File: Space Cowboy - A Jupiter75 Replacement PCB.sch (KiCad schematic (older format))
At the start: 203 parts, among them SW1 SW_PUSH, U1 ATmega32U4-AU, Y1 16MHz

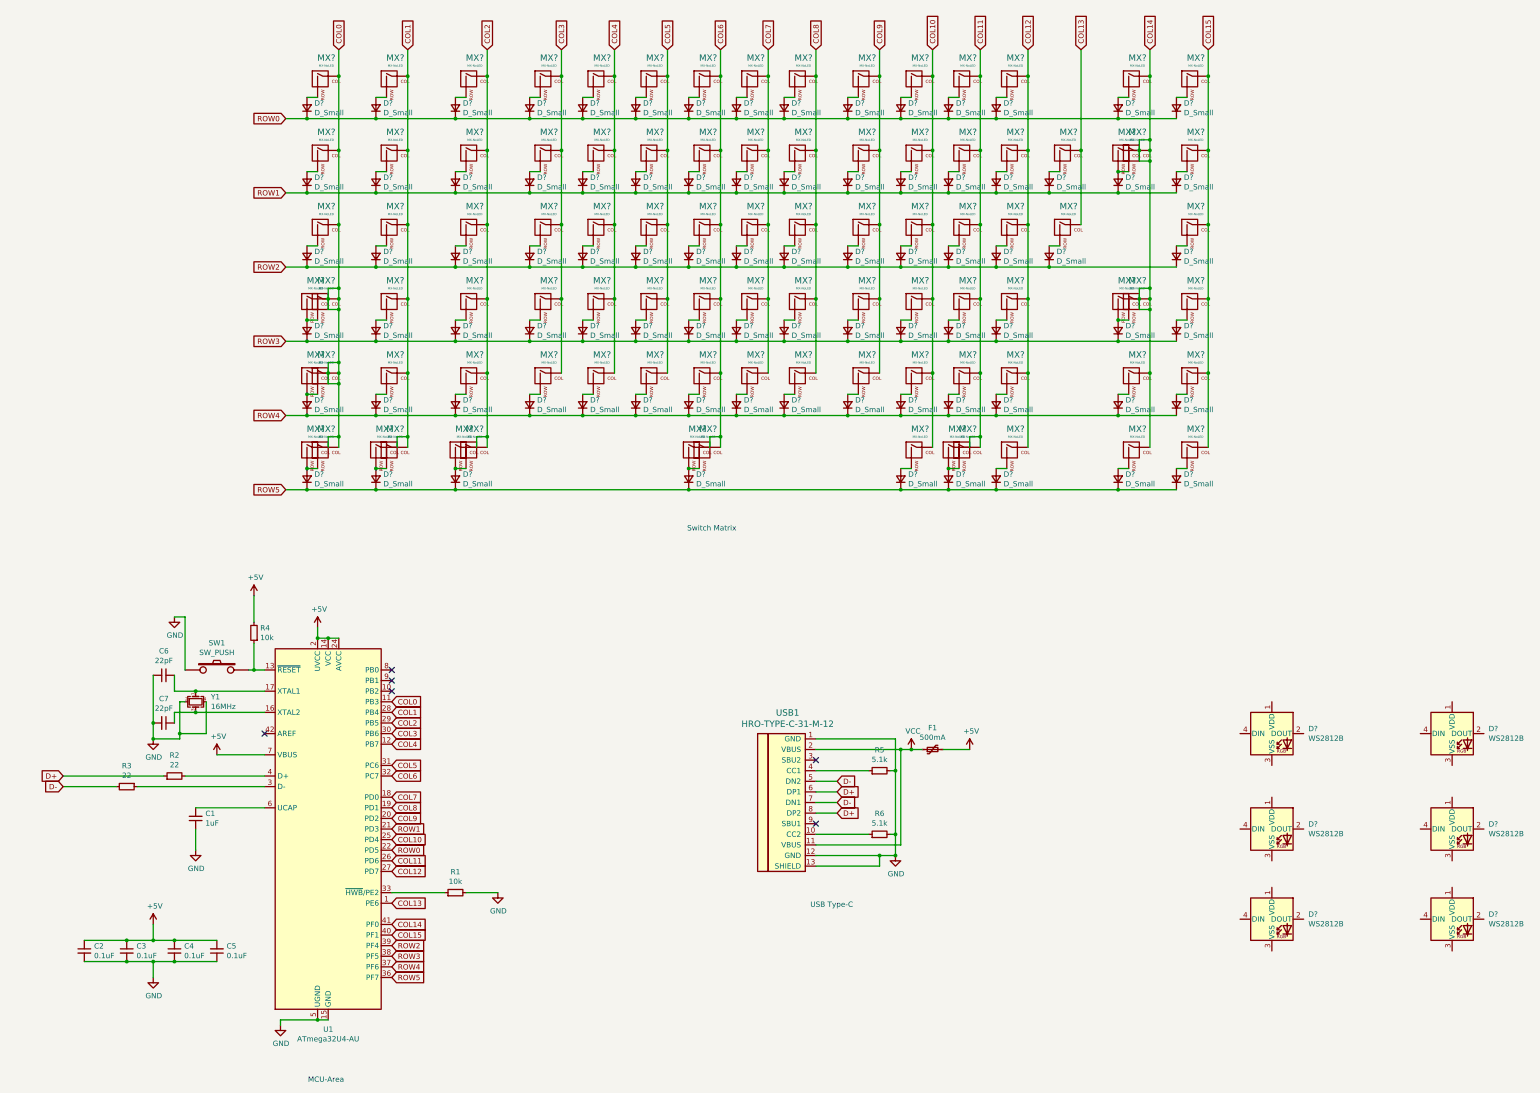
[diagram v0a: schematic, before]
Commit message: Update Space Cowboy - A Jupiter75 Replacement PCB.sch
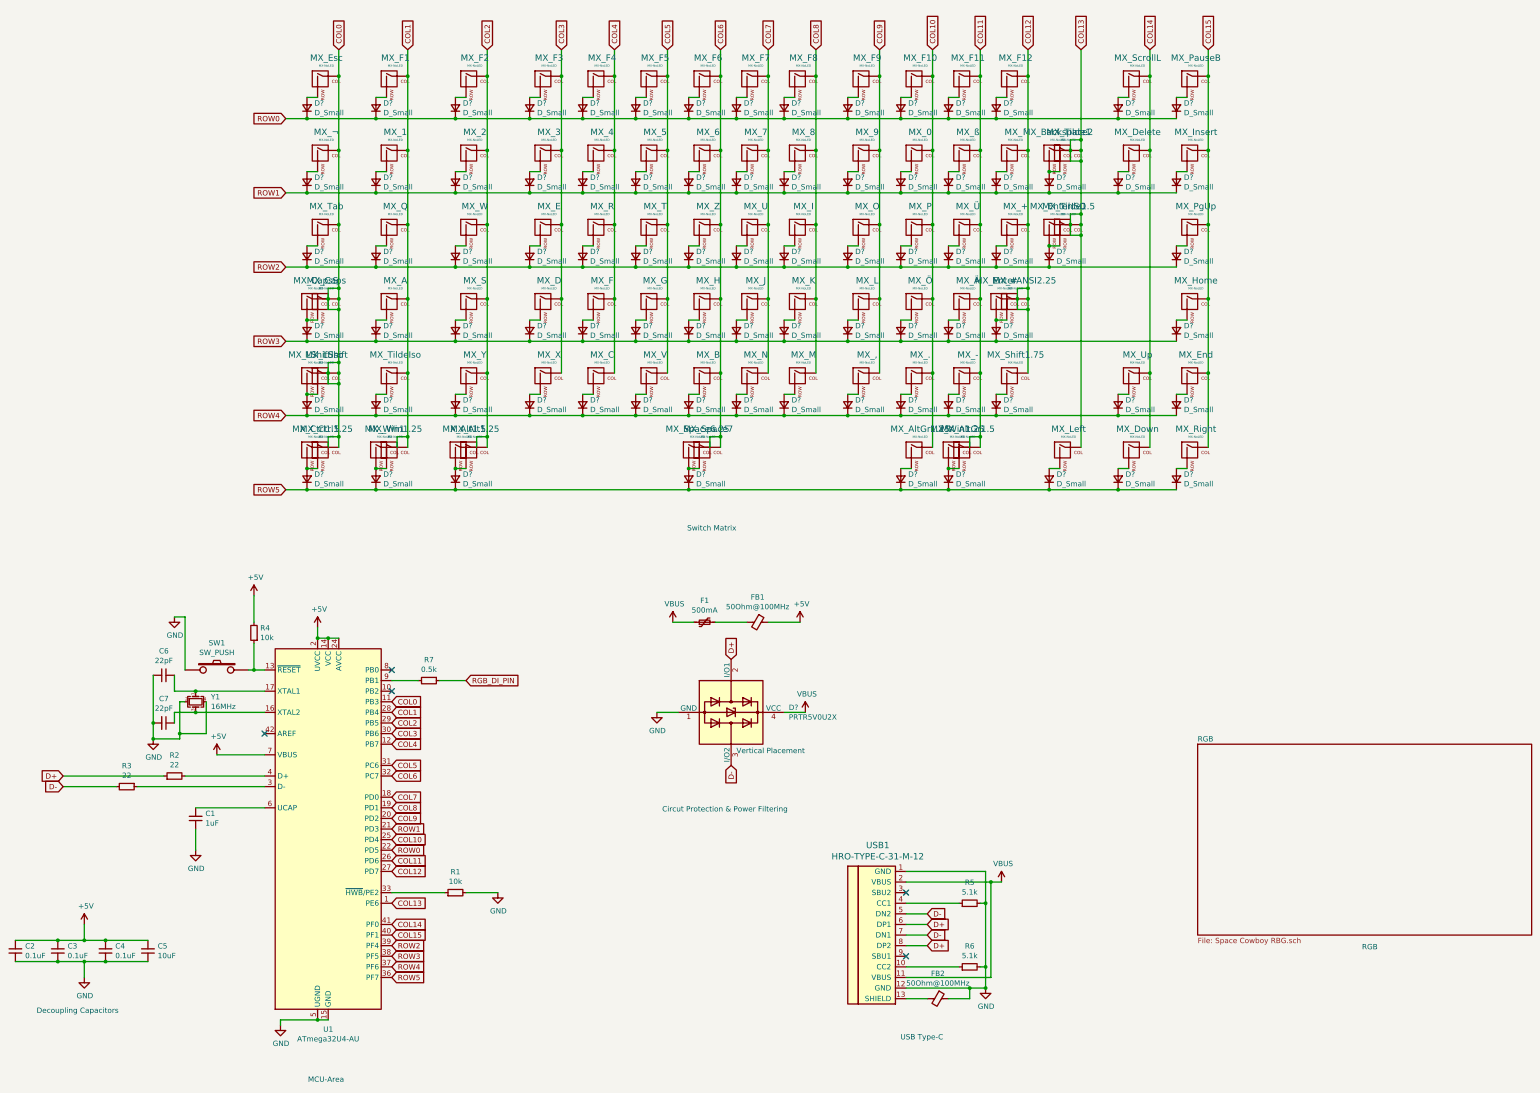
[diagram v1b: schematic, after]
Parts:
- removed D? (x6): WS2812B, LED_SMD:LED_WS2812B_PLCC4_5.0x5.0mm_P3.2mm, symbol LED:WS2812B
- removed D?: D_Small, symbol Device:D_Small
- removed MX? (x4): MX-NoLED, symbol MX_Alps_Hybrid:MX-NoLED
- added D?: PRTR5V0U2X, Package_TO_SOT_SMD:SOT-143, symbol Power_Protection:PRTR5V0U2X
- added FB1, FB2: 50Ohm@100MHz, symbol Device:Ferrite_Bead_Small
- added MX_#, MX_Backspace2, MX_Delete, MX_EnterISO: MX-NoLED, symbol MX_Alps_Hybrid:MX-NoLED
- added R7: 0.5k, symbol Device:R_Small
- C5: value 0.1uF -> 10uF
- gave numbers to parts that had none: 89
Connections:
- net +5V: now also FB1.1; no longer F1.2
- net COL12: now also MX_#.1 (COL); no longer MX_Left.1 (COL)
- net COL13: now also MX_Left.1 (COL), MX_Backspace2.1 (COL), MX_EnterISO.1 (COL)
- net COL14: now also MX_Delete.1 (COL)
- net D+: now also D?.2 (I/O1)
- net D-: now also D?.3 (I/O2)
- net GND: now also D?.1 (GND), FB2.1; no longer USB1.13 (SHIELD)
- net at U1.9 (PB1): now also R7.2
- net at D?.2 (A), MX_Tilde1.2 (ROW): now also MX_Backspace2.2 (ROW)
- net at D?.2 (A): now also MX_Delete.2 (ROW)
- net at D?.2 (A), MX_Tilde1.5.2 (ROW): now also MX_EnterISO.2 (ROW)
- net at D?.2 (A), MX_EnterANSI2.25.2 (ROW): now also MX_#.2 (ROW)
- net VCC renamed VBUS
- net VBUS: now also D?.4 (VCC)
- new net: FB2.2, USB1.13 (SHIELD)
- new net: F1.2, FB1.2
- new net RGB_DI_PIN: R7.1
- no-connect marks 6 -> 5
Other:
- note added: "Circut Protection & Power Filtering"
- note added: "Decoupling Capacitors"
- note added: "RGB"
- note added: "Vertical Placement"
- moved on the sheet: C2, C3, C4, C5, D?, F1, MX_Left, R5, R6, USB1

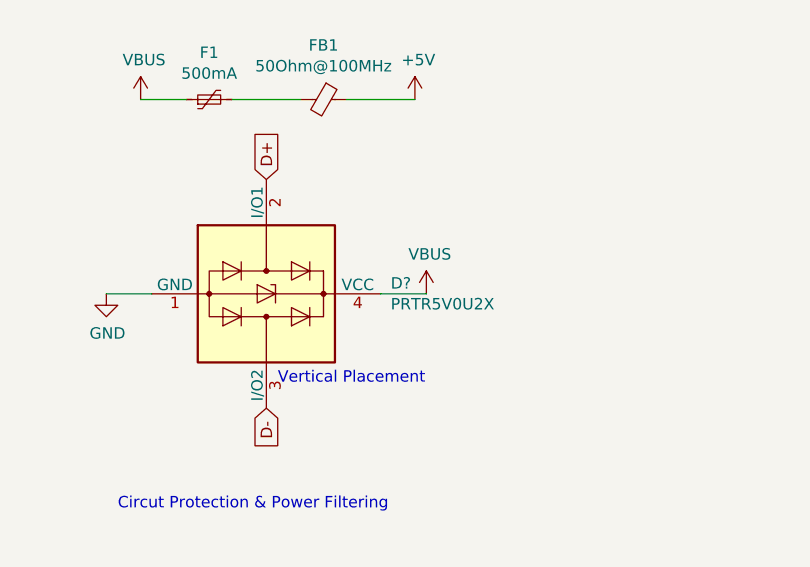
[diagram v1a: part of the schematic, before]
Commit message: Update Space Cowboy - A Jupiter75 Replacement PCB.sch
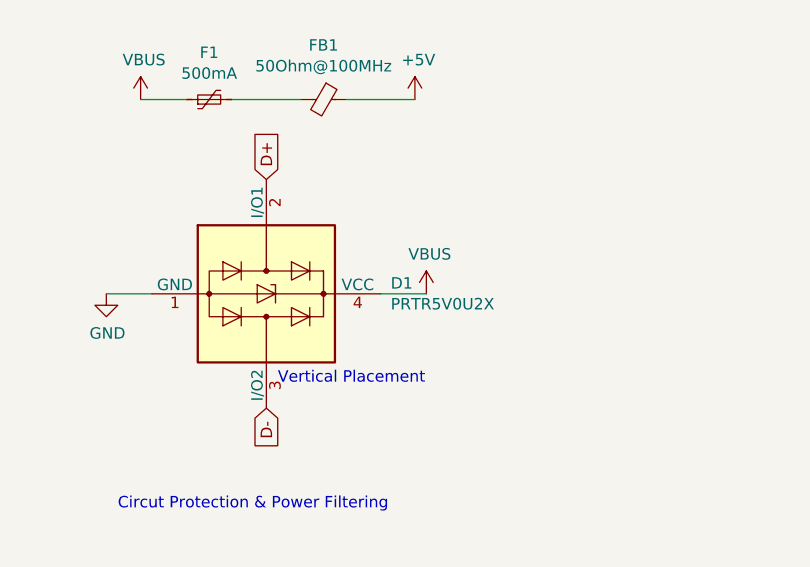
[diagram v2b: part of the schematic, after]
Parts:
- gave numbers to parts that had none: 1
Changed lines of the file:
@@
 D+
 $Comp
-L Power_Protection:PRTR5V0U2X D?
+L Power_Protection:PRTR5V0U2X D1
 U 1 1 5FEA96D8
 P 7950 7400
-F 0 "D?" V 7904 7944 50  0000 L CNN
+F 0 "D1" V 7904 7944 50  0000 L CNN
 F 1 "PRTR5V0U2X" V 7995 7944 50  0000 L CNN
 F 2 "Package_TO_SOT_SMD:SOT-143" H 8010 7400 50  0001 C CNN

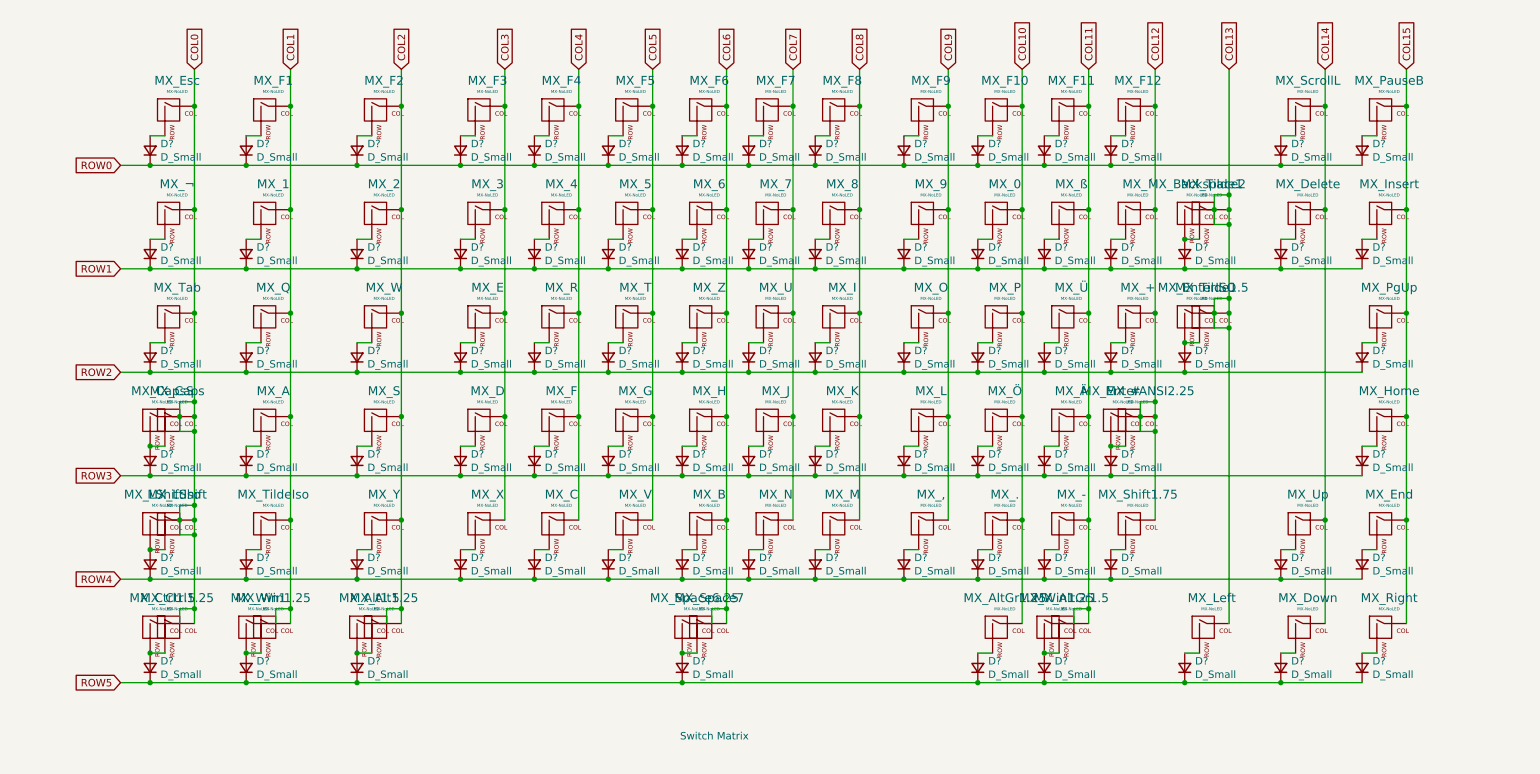
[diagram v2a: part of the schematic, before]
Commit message: Update Space Cowboy - A Jupiter75 Replacement PCB.sch
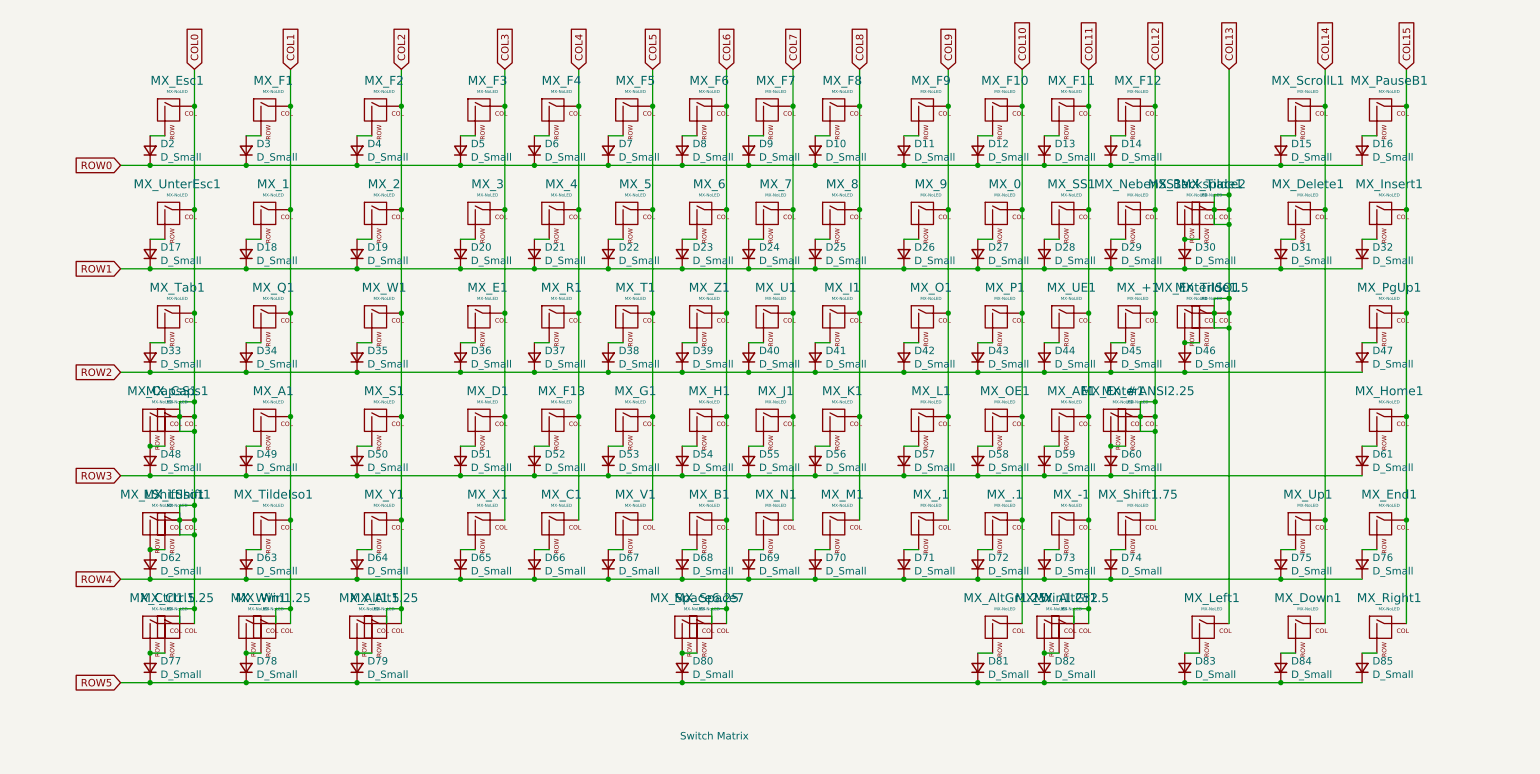
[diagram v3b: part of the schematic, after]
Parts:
- C1, C2, C3, C4, C5, C6, C7: footprint (none) -> Capacitors_SMD:C_0603
- D1: footprint Package_TO_SOT_SMD:SOT-143 -> PRTR5V0U2X:SOT190P230X110-4N
- D10, D11, D12, D13, D14, D15, D16, D17, D18, D19, D2, D20, D21, D22, D23, D24, D25, D26, D27, D28, D29, D3, D30, D31, D32, D33, D34, D35, D36, D37, D38, D39, D4, D40, D41, D42, D43, D44, D45, D46, D47, D48, D49, D5, D50, D51, D52, D53, D54, D55, D56, D57, D58, D59, D6, D60, D61, D62, D63, D64, D65, D66, D67, D68, D69, D7, D70, D71, D72, D73, D74, D75, D76, D77, D78, D79, D8, D80, D81, D82, D83, D84, D85, D9: renamed from D?; footprint (none) -> Diodes_SMD:D_SOD-123
- F1: footprint (none) -> Fuse_Holders_and_Fuses:Fuse_SMD1206_Reflow
- FB1, FB2: footprint (none) -> Ferrite Bead 742792114:BEADC3216X130N
- MX_#1: renamed from MX_#; footprint (none) -> Keyboard_Mine:MXOnly-1U
- MX_+1: renamed from MX_+; footprint (none) -> Keyboard_Mine:MXOnly-1U
- MX_,1: renamed from MX_,; footprint (none) -> Keyboard_Mine:MXOnly-1U
- MX_-1: renamed from MX_-; footprint (none) -> Keyboard_Mine:MXOnly-1U
- MX_.1: renamed from MX_.; footprint (none) -> Keyboard_Mine:MXOnly-1U
- MX_0, MX_1, MX_2, MX_3, MX_4, MX_5, MX_6, MX_7, MX_8, MX_9, MX_F1, MX_F10, MX_F11, MX_F12, MX_F2, MX_F3, MX_F4, MX_F5, MX_F6, MX_F7, MX_F8, MX_F9, MX_Tilde1, MX_Win1: footprint (none) -> Keyboard_Mine:MXOnly-1U
- MX_A1: renamed from MX_A; footprint (none) -> Keyboard_Mine:MXOnly-1U
- MX_AE1: renamed from MX_Ä; footprint (none) -> Keyboard_Mine:MXOnly-1U
- MX_Alt1.25, MX_AltGr1.25, MX_Ctrl1.25, MX_Win1.25: footprint (none) -> Keyboard_Mine:MXOnly-1.25U
- MX_Alt1.5, MX_AltGr1.5, MX_Ctrl1.5, MX_Tilde1.5: footprint (none) -> Keyboard_Mine:MXOnly-1.5U
- MX_B1: renamed from MX_B; footprint (none) -> Keyboard_Mine:MXOnly-1U
- MX_Backspace2: footprint (none) -> Keyboard_Mine:MXOnly-2U
- MX_C1: renamed from MX_C; footprint (none) -> Keyboard_Mine:MXOnly-1U
- MX_Caps1: renamed from MX_Caps; footprint (none) -> Keyboard_Mine:MXOnly-1.75U
- MX_CapsS1: renamed from MX_CapsS; footprint (none) -> Keyboard_Mine:MXOnly-1.75U
- MX_D1: renamed from MX_D; footprint (none) -> Keyboard_Mine:MXOnly-1U
- MX_Delete1: renamed from MX_Delete; footprint (none) -> Keyboard_Mine:MXOnly-1U
- MX_Down1: renamed from MX_Down; footprint (none) -> Keyboard_Mine:MXOnly-1U
- MX_E1: renamed from MX_E; footprint (none) -> Keyboard_Mine:MXOnly-1U
- MX_End1: renamed from MX_End; footprint (none) -> Keyboard_Mine:MXOnly-1U
- MX_EnterANSI2.25: footprint (none) -> Keyboard_Mine:MXOnly-2.25U
- MX_EnterISO1: renamed from MX_EnterISO; footprint (none) -> Keyboard_Mine:MX-ISO
- MX_Esc1: renamed from MX_Esc; footprint (none) -> Keyboard_Mine:MXOnly-1U
- MX_F13: renamed from MX_F; footprint (none) -> Keyboard_Mine:MXOnly-1U
- MX_G1: renamed from MX_G; footprint (none) -> Keyboard_Mine:MXOnly-1U
- MX_H1: renamed from MX_H; footprint (none) -> Keyboard_Mine:MXOnly-1U
- MX_Home1: renamed from MX_Home; footprint (none) -> Keyboard_Mine:MXOnly-1U
- MX_I1: renamed from MX_I; footprint (none) -> Keyboard_Mine:MXOnly-1U
- MX_Insert1: renamed from MX_Insert; footprint (none) -> Keyboard_Mine:MXOnly-1U
- MX_J1: renamed from MX_J; footprint (none) -> Keyboard_Mine:MXOnly-1U
- MX_K1: renamed from MX_K; footprint (none) -> Keyboard_Mine:MXOnly-1U
- MX_L1: renamed from MX_L; footprint (none) -> Keyboard_Mine:MXOnly-1U
- MX_LShift1: renamed from MX_LShift; footprint (none) -> Keyboard_Mine:MXOnly-2.25U
- MX_LShiftIso1: renamed from MX_LShiftIso; footprint (none) -> Keyboard_Mine:MXOnly-1.25U
- MX_Left1: renamed from MX_Left; footprint (none) -> Keyboard_Mine:MXOnly-1U
- MX_M1: renamed from MX_M; footprint (none) -> Keyboard_Mine:MXOnly-1U
- MX_N1: renamed from MX_N; footprint (none) -> Keyboard_Mine:MXOnly-1U
- MX_NebenSS1: renamed from MX_´; footprint (none) -> Keyboard_Mine:MXOnly-1U
- MX_O1: renamed from MX_O; footprint (none) -> Keyboard_Mine:MXOnly-1U
- MX_OE1: renamed from MX_Ö; footprint (none) -> Keyboard_Mine:MXOnly-1U
- MX_P1: renamed from MX_P; footprint (none) -> Keyboard_Mine:MXOnly-1U
- MX_PauseB1: renamed from MX_PauseB; footprint (none) -> Keyboard_Mine:MXOnly-1U
- MX_PgUp1: renamed from MX_PgUp; footprint (none) -> Keyboard_Mine:MXOnly-1U
- MX_Q1: renamed from MX_Q; footprint (none) -> Keyboard_Mine:MXOnly-1U
- MX_R1: renamed from MX_R; footprint (none) -> Keyboard_Mine:MXOnly-1U
- MX_Right1: renamed from MX_Right; footprint (none) -> Keyboard_Mine:MXOnly-1U
- MX_S1: renamed from MX_S; footprint (none) -> Keyboard_Mine:MXOnly-1U
- MX_SS1: renamed from MX_ß; footprint (none) -> Keyboard_Mine:MXOnly-1U
- MX_ScrollL1: renamed from MX_ScrollL; footprint (none) -> Keyboard_Mine:MXOnly-1U
- MX_Shift1.75: footprint (none) -> Keyboard_Mine:MXOnly-1.75U
- MX_Space6.25: footprint (none) -> Keyboard_Mine:MXOnly-6U-ReversedStabilizers
- MX_Space7: footprint (none) -> Keyboard_Mine:MXOnly-7U-ReversedStabilizers_NoLED
- MX_T1: renamed from MX_T; footprint (none) -> Keyboard_Mine:MXOnly-1U
- MX_Tab1: renamed from MX_Tab; footprint (none) -> Keyboard_Mine:MXOnly-1.5U
- MX_TildeIso1: renamed from MX_TildeIso; footprint (none) -> Keyboard_Mine:MXOnly-1U
- MX_U1: renamed from MX_U; footprint (none) -> Keyboard_Mine:MXOnly-1U
- MX_UE1: renamed from MX_Ü; footprint (none) -> Keyboard_Mine:MXOnly-1U
- MX_UnterEsc1: renamed from MX_¬; footprint (none) -> Keyboard_Mine:MXOnly-1U
- MX_Up1: renamed from MX_Up; footprint (none) -> Keyboard_Mine:MXOnly-1U
- MX_V1: renamed from MX_V; footprint (none) -> Keyboard_Mine:MXOnly-1U
- MX_W1: renamed from MX_W; footprint (none) -> Keyboard_Mine:MXOnly-1U
- MX_Win1.252: renamed from MX_Win1.25; footprint (none) -> Keyboard_Mine:MXOnly-1.25U
- MX_X1: renamed from MX_X; footprint (none) -> Keyboard_Mine:MXOnly-1U
- MX_Y1: renamed from MX_Y; footprint (none) -> Keyboard_Mine:MXOnly-1U
- MX_Z1: renamed from MX_Z; footprint (none) -> Keyboard_Mine:MXOnly-1U
- R1, R2, R3, R4, R5, R6, R7: footprint (none) -> Resistors_SMD:R_0603
- SW1: footprint (none) -> random-keyboard-parts:SKQG-1155865
- U1: footprint Package_QFP:TQFP-44_10x10mm_P0.8mm -> Keyboard_Mine:ATMEGA32U4_AU
- USB1: footprint (none) -> Type-C:HRO-TYPE-C-31-M-12
- Y1: footprint (none) -> Crystals:Crystal_SMD_3225-4pin_3.2x2.5mm

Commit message: Update Space Cowboy - A Jupiter75 Replacement PCB.sch
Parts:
- MX_Space6.25: footprint Keyboard_Mine:MXOnly-6U-ReversedStabilizers -> Keyboard_Mine:MXOnlyNoLED-6.25U-ReversedStabilizers
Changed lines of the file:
@@
 F 0 "MX_Space6.25" H 7633 5173 60  0000 C CNN
 F 1 "MX-NoLED" H 7633 5099 20  0000 C CNN
-F 2 "Keyboard_Mine:MXOnly-6U-ReversedStabilizers" H 6975 4925 60  0001 C CNN
+F 2 "Keyboard_Mine:MXOnlyNoLED-6.25U-ReversedStabilizers" H 6975 4925 60  0001 C CNN
 F 3 "" H 6975 4925 60  0001 C CNN
 	1    7600 4950

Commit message: Update Space Cowboy - A Jupiter75 Replacement PCB.sch
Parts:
- MX_EnterISO1: footprint Keyboard_Mine:MX-ISO -> Keyboard_Mine:MXOnly-2U
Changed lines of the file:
@@
 F 0 "MX_EnterISO1" H 11033 3073 60  0000 C CNN
 F 1 "MX-NoLED" H 11033 2999 20  0000 C CNN
-F 2 "Keyboard_Mine:MX-ISO" H 10375 2825 60  0001 C CNN
+F 2 "Keyboard_Mine:MXOnly-2U" H 10375 2825 60  0001 C CNN
 F 3 "" H 10375 2825 60  0001 C CNN
 	1    11000 2850
